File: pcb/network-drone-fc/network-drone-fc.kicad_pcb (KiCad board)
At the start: 4 copper layers, 36 x 39 mm, 84 parts, among them J1 U.FL-R-SMT-1, J2 TYPE-C 16PIN 2MD, J3 U.FL GPS, J4 ESC, J5 Sensor port 5V I2C, J6 Radio UART 5V, J7 Charging board, U1 ESP32-S3FN8, U2 USBLC6-2SC6, U3 AP63205WU-7, U4 TLV75733PDRVR, U5 TPS7A2033PDBVR, U6 ICM-42688-P, U7 BMP581, U8 MAX-M10S, X1 Q22FA12800101

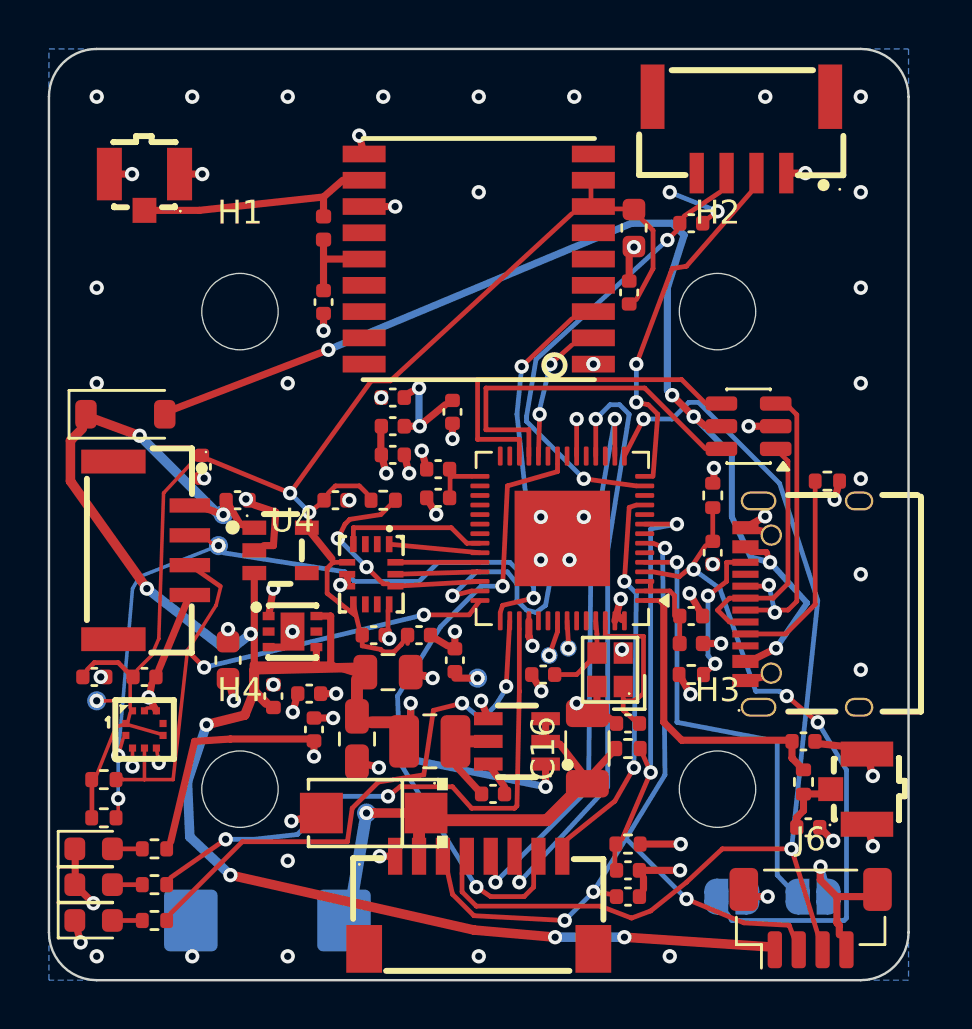
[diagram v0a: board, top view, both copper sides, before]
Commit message: PCB: chamfer the 16 right-angle track corners into 45 degree bends
USB pair, crystal, IMU interrupt, CC2 and a few power links. No corner on the board is now 100 degrees or sharper. DRC 0 errors; schematic and board still match on all 296 pins.
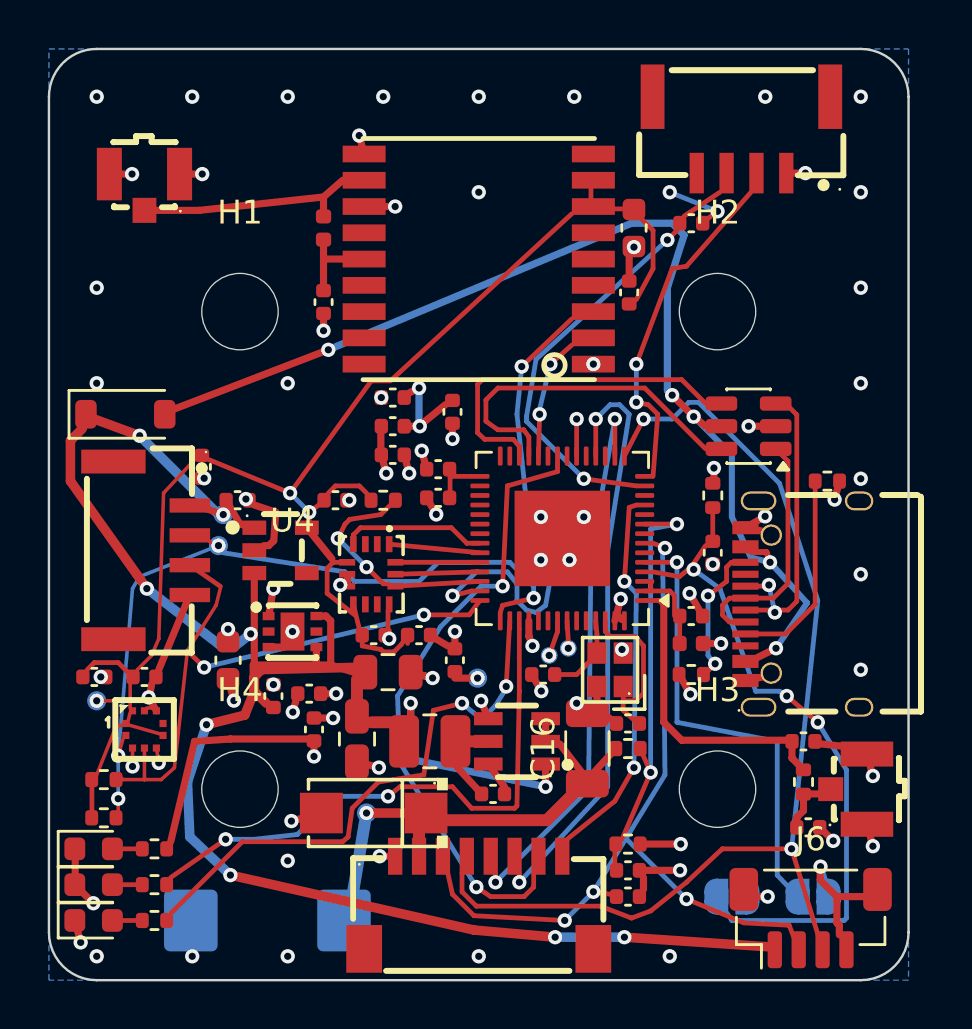
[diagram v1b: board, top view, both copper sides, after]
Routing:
- net USB_DN: track 14.9 -> 14.2 mm
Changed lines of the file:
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@@
 	)
 	(segment
-		(start 91.4 99.8)
+		(start 91.2 99.8)
 		(end 91 99.8)
 		(width 0.3)
@@
 	(segment
 		(start 91.5 98.4)
-		(end 91.4 99.8)
+		(end 91.414249 99.600508)
 		(width 0.3)
 		(layer "F.Cu")
@@
 	)
 	(segment
+		(start 91.2 99.8)
+		(end 91.414249 99.600508)
+		(width 0.3)
+		(layer "F.Cu")
+		(net 2)
+	)
+	(segment
 		(start 114.28 111.6)
 		(end 114.845685 112.165685)
@@
 	)
 	(segment
+		(start 110.212132 102.287867)
+		(end 110.212132 102.712132)
+		(width 0.2)
+		(layer "F.Cu")
+		(net 7)
+	)
+	(segment
 		(start 110.5 102)
-		(end 110 102.5)
+		(end 110.212132 102.287867)
 		(width 0.2)
 		(layer "F.Cu")
@@
 	)
 	(segment
-		(start 110 102.5)
+		(start 110.212132 102.712132)
 		(end 110.5 103)
 		(width 0.2)
@@
 	)
 	(segment
-		(start 100.3 93.2)
-		(end 100.3 94.95)
+		(start 100.3 93.7)
+		(end 100.3 94.592857)
 		(width 0.2)
 		(layer "F.Cu")
@@
 	)
 	(segment
-		(start 102.1 94.95)
+		(start 102.1 95.25)
 		(end 102.1 96.05)
 		(width 0.2)
@@
 	(segment
 		(start 106.95 93.2)
-		(end 100.3 93.2)
+		(end 100.8 93.2)
+		(width 0.2)
+		(layer "F.Cu")
+		(net 8)
+	)
+	(segment
+		(start 100.8 94.95)
+		(end 101.883333 94.95)
+		(width 0.2)
+		(layer "F.Cu")
+		(net 8)
+	)
+	(segment
+		(start 100.3 93.7)
+		(end 100.8 93.2)
 		(width 0.2)
 		(layer "F.Cu")
@@
 	)
 	(segment
-		(start 100.3 94.95)
-		(end 102.1 94.95)
+		(start 100.3 94.592857)
+		(end 100.8 94.95)
+		(width 0.2)
+		(layer "F.Cu")
+		(net 8)
+	)
+	(segment
+		(start 102.1 95.25)
+		(end 101.883333 94.95)
 		(width 0.2)
 		(layer "F.Cu")
@@
 	)
 	(segment
+		(start 100.15 92.85)
+		(end 99.95 93.05)
+		(width 0.2)
+		(layer "F.Cu")
+		(net 10)
+	)
+	(segment
 		(start 108.5 92.85)
-		(end 99.95 92.85)
+		(end 100.15 92.85)
 		(width 0.2)
 		(layer "F.Cu")
@@
 	)
 	(segment
-		(start 99.95 95.35)
-		(end 101.7 95.35)
+		(start 100.25 95.35)
+		(end 99.95 95.074)
 		(width 0.2)
 		(layer "F.Cu")
@@
 	)
 	(segment
-		(start 101.7 95.35)
+		(start 100.25 95.35)
+		(end 101.451428 95.35)
+		(width 0.2)
+		(layer "F.Cu")
+		(net 10)
+	)
+	(segment
+		(start 101.7 95.649999)
 		(end 101.7 96.05)
 		(width 0.2)
@@
 	)
 	(segment
+		(start 101.451428 95.35)
+		(end 101.7 95.649999)
+		(width 0.2)
+		(layer "F.Cu")
+		(net 10)
+	)
+	(segment
 		(start 109.5 93.85)
 		(end 108.5 92.85)
@@
 	)
 	(segment
-		(start 99.95 92.85)
-		(end 99.95 95.35)
+		(start 99.95 93.05)
+		(end 99.95 95.074)
 		(width 0.2)
 		(layer "F.Cu")
@@
 	)
 	(segment
+		(start 90.899915 104.992859)
+		(end 90.6 105.3)
+		(width 0.4)
+		(layer "F.Cu")
+		(net 11)
+	)
+	(segment
 		(start 90.6 105.9)
 		(end 90.2 106.9)
@@
 	(segment
 		(start 94.8 104.9)
-		(end 90.6 105)
+		(end 90.899915 104.992859)
 		(width 0.4)
 		(layer "F.Cu")
@@
 	(segment
 		(start 93.8 104.8)
-		(end 93.8 102.75)
+		(end 93.8 102.95)
 		(width 0.3)
 		(layer "F.Cu")
@@
 	)
 	(segment
-		(start 90.6 105)
+		(start 90.6 105.3)
 		(end 90.6 105.9)
 		(width 0.4)
@@
 	)
 	(segment
+		(start 93.8 102.95)
+		(end 93.6 102.75)
+		(width 0.3)
+		(layer "F.Cu")
+		(net 11)
+	)
+	(segment
 		(start 90 98.9)
 		(end 90.6 99.05)
@@
 	)
 	(segment
-		(start 93.8 102.75)
+		(start 93.6 102.75)
 		(end 93.2 102.75)
 		(width 0.3)
@@
 	(segment
 		(start 90.1 112.2)
-		(end 94.5 112.2)
+		(end 94.3 112.2)
 		(width 0.2)
 		(layer "F.Cu")
@@
 	)
 	(segment
-		(start 94.5 112.2)
+		(start 94.528284 112.00201)
 		(end 94.7 110.8)
 		(width 0.2)
@@
 	)
 	(segment
+		(start 94.3 112.2)
+		(end 94.528284 112.00201)
+		(width 0.2)
+		(layer "F.Cu")
+		(net 15)
+	)
+	(segment
 		(start 94.7 110.8)
 		(end 95.8 109.7)
@@
 	)
 	(segment
-		(start 110.38 100.5)
+		(start 110.38 100.7)
 		(end 110.38 101.3)
 		(width 0.2)
@@
 	(segment
 		(start 111.17 100.5)
-		(end 110.38 100.5)
+		(end 110.58 100.5)
+		(width 0.2)
+		(layer "F.Cu")
+		(net 16)
+	)
+	(segment
+		(start 110.38 100.7)
+		(end 110.58 100.5)
 		(width 0.2)
 		(layer "F.Cu")
@@
 	(segment
 		(start 98.85 99.05)
-		(end 94.75 99.05)
+		(end 95.05 99.05)
 		(width 0.2)
 		(layer "F.Cu")
@@
 	)
 	(segment
-		(start 94.75 99.05)
+		(start 95.05 99.05)
+		(end 94.75 99.35)
+		(width 0.2)
+		(layer "F.Cu")
+		(net 30)
+	)
+	(segment
+		(start 94.75 99.35)
 		(end 94.75 99.74)
 		(width 0.2)
@@
 	)
 	(segment
-		(start 87.2 109.6)
+		(start 86.7 109.6)
 		(end 86 109.6)
 		(width 0.15)
@@
 	)
 	(segment
+		(start 86.7 109.6)
+		(end 87.255215 109.103058)
+		(width 0.15)
+		(layer "F.Cu")
+		(net 35)
+	)
+	(segment
 		(start 88.5 104.9)
 		(end 87.8 104.2)
@@
 	(segment
 		(start 87.8 104.2)
-		(end 87.2 109.6)
+		(end 87.255215 109.103058)
 		(width 0.15)
 		(layer "F.Cu")
@@
 	(segment
 		(start 105.3 102.95)
-		(end 105.3 103.6)
+		(end 105.3 103.399999)
 		(width 0.2)
 		(layer "F.Cu")
@@
 	)
 	(segment
-		(start 106.9 103.6)
+		(start 106.9 104)
 		(end 106.9 106)
 		(width 0.2)
@@
 	)
 	(segment
-		(start 105.3 103.6)
-		(end 106.9 103.6)
+		(start 105.5 103.6)
+		(end 106.55 103.6)
 		(width 0.2)
 		(layer "F.Cu")
@@
 	)
 	(segment
+		(start 106.9 104)
+		(end 106.55 103.6)
+		(width 0.2)
+		(layer "F.Cu")
+		(net 42)
+	)
+	(segment
 		(start 106.05 106.3)
 		(end 106.05 105.7)
 		(width 0.2)
 		(layer "F.Cu")
+		(net 42)
+	)
+	(segment
+		(start 105.3 103.399999)
+		(end 105.5 103.6)
+		(width 0.2)
+		(layer "F.Cu")

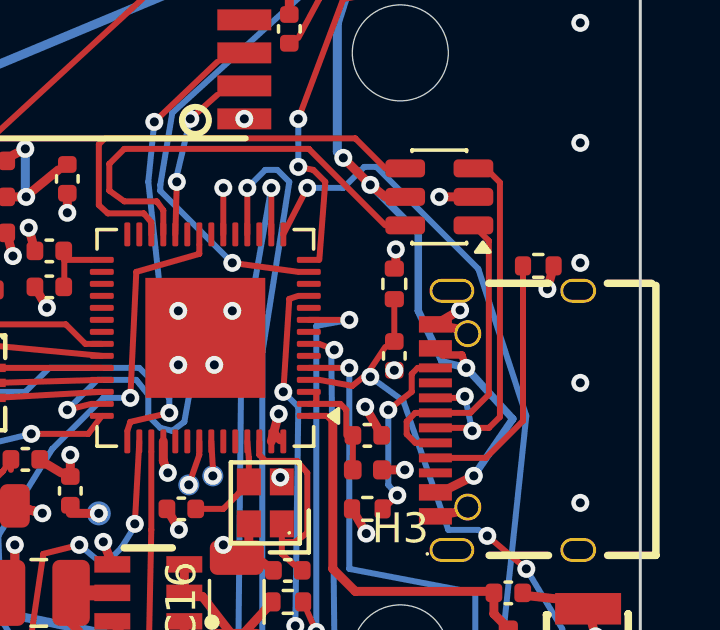
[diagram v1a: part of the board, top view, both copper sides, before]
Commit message: PCB: ground via moved clear of the USB socket's slot; footprint library links and unused-pin net names synced with the schematic
The via was 0.20 mm from the slot wall and is now 0.26 mm (fab minimum 0.25). The rest is bookkeeping with no copper change: KiCad's schematic parity check drops from 140 items to 2, both the USB socket's grounded locating pegs.
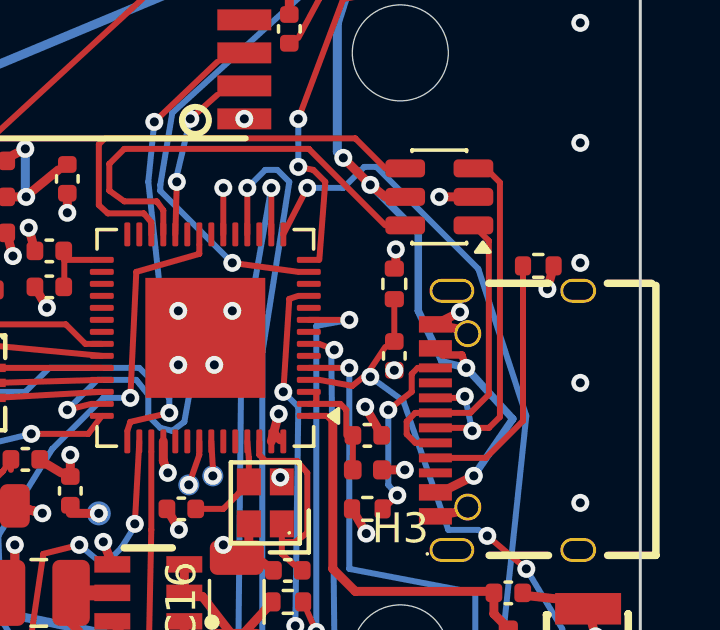
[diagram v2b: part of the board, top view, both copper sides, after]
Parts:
- C1, C10, C11, C12, C13, C14, C15, C17, C2, C20, C21, C22, C23, C24, C25, C26, C27, C28, C29, C3, C31, C32, C33, C34, C5, C6, C7, C8, C9: footprint C_0402_1005Metric -> Capacitor_SMD:C_0402_1005Metric
- C16: footprint C_1206_3216Metric -> Capacitor_SMD:C_0805_2012Metric
- C18, C19: footprint C_0805_2012Metric -> Capacitor_SMD:C_0805_2012Metric
- C30, C4: footprint C_0603_1608Metric -> Capacitor_SMD:C_0603_1608Metric
- C35: footprint CP_EIA-7343-31_Kemet-D_HandSolder -> Capacitor_Tantalum_SMD:CP_EIA-7343-31_Kemet-D_HandSolder
- D1: footprint D_SOD-123 -> Diode_SMD:D_SOD-123
- D2, D3, D4: footprint LED_0603_1608Metric -> LED_SMD:LED_0603_1608Metric
- D5: footprint SMA_L4.4-W2.6-LS5.0-RD -> tar_fc:SMA_L4.4-W2.6-LS5.0-RD
- J1, J3: footprint RF-SMD_FRF05002-JSS103M -> tar_fc:RF-SMD_FRF05002-JSS103M
- J2: footprint USB-C-SMD_TYPE-C-16PIN-2MD-073 -> tar_fc:USB-C-SMD_TYPE-C-16PIN-2MD-073
- J4: footprint CONN-TH_SM08B-SRSS-TB-LF-SN -> tar_fc:CONN-TH_SM08B-SRSS-TB-LF-SN
- J5, J7: footprint CONN-SMD_4P-P1.25_SM04B-GHS-TB-LF-SN -> tar_fc:CONN-SMD_4P-P1.25_SM04B-GHS-TB-LF-SN
- L1, L3: footprint L_0402_1005Metric -> Inductor_SMD:L_0402_1005Metric
- L2: footprint L_1008_2520Metric -> Inductor_SMD:L_1008_2520Metric
- R1, R10, R11, R12, R13, R3, R4, R5, R6, R7, R8, R9: footprint R_0402_1005Metric -> Resistor_SMD:R_0402_1005Metric
- TP1, TP2, TP3, TP4, TP5, TP6: footprint TestPoint_Pad_D1.0mm -> TestPoint:TestPoint_Pad_D1.0mm
- U1: footprint QFN-56-1EP_7x7mm_P0.4mm_EP4x4mm -> Package_DFN_QFN:QFN-56-1EP_7x7mm_P0.4mm_EP4x4mm
- U2: footprint SOT-23-6 -> Package_TO_SOT_SMD:SOT-23-6
- U3: footprint TSOT-23-6_L2.9-W1.6-P0.95-LS2.8-BL -> tar_fc:TSOT-23-6_L2.9-W1.6-P0.95-LS2.8-BL
- U4: footprint TDFN-6_L2.0-W2.0-P0.65-TL-EP -> tar_fc:TDFN-6_L2.0-W2.0-P0.65-TL-EP
- U5: footprint SOT-23-5_L2.9-W1.6-P0.95-LS2.8-BR -> tar_fc:SOT-23-5_L2.9-W1.6-P0.95-LS2.8-BR
- U6: footprint LGA-14_L3.0-W2.5-P0.50-TL -> tar_fc:LGA-14_L3.0-W2.5-P0.50-TL
- U7: footprint LGA-10_L2.0-W2.0-P0.50-TL_BMP581 -> tar_fc:LGA-10_L2.0-W2.0-P0.50-TL_BMP581
- U8: footprint SMD-18_L10.1-W9.7-P1.10-TL_SKG09F -> tar_fc:SMD-18_L10.1-W9.7-P1.10-TL_SKG09F
- X1: footprint CRYSTAL-SMD_4P-L2.0-W1.6-BL -> tar_fc:CRYSTAL-SMD_4P-L2.0-W1.6-BL
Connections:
- J2 pad A8: (no net) -> unconnected-(J2-SBU1-PadA8)
- J2 pad B8: (no net) -> unconnected-(J2-SBU2-PadB8)
- J4 pad 10: (no net) -> unconnected-(J4-Pad10)
- J4 pad 9: (no net) -> unconnected-(J4-Pad9)
- J5 pad 5: (no net) -> unconnected-(J5-Pad5)
- J5 pad 6: (no net) -> unconnected-(J5-Pad6)
- J7 pad 4: (no net) -> unconnected-(J7-Pad4)
- J7 pad 5: (no net) -> unconnected-(J7-Pad5)
- J7 pad 6: (no net) -> unconnected-(J7-Pad6)
- U1 pad 10: (no net) -> unconnected-(U1-GPIO5-Pad10)
- U1 pad 12: (no net) -> unconnected-(U1-GPIO7-Pad12)
- U1 pad 17: (no net) -> unconnected-(U1-GPIO12-Pad17)
- U1 pad 19: (no net) -> unconnected-(U1-GPIO14-Pad19)
- U1 pad 21: (no net) -> unconnected-(U1-XTAL_32K_P-Pad21)
- U1 pad 23: (no net) -> unconnected-(U1-GPIO17-Pad23)
- U1 pad 27: (no net) -> unconnected-(U1-GPIO21-Pad27)
- U1 pad 28: (no net) -> unconnected-(U1-SPICS1-Pad28)
- U1 pad 30: (no net) -> unconnected-(U1-SPIHD-Pad30)
- U1 pad 31: (no net) -> unconnected-(U1-SPIWP-Pad31)
- U1 pad 32: (no net) -> unconnected-(U1-SPICS0-Pad32)
- U1 pad 33: (no net) -> unconnected-(U1-SPICLK-Pad33)
- U1 pad 34: (no net) -> unconnected-(U1-SPIQ-Pad34)
- U1 pad 35: (no net) -> unconnected-(U1-SPID-Pad35)
- U1 pad 47: (no net) -> unconnected-(U1-MTDI-Pad47)
- U1 pad 48: (no net) -> unconnected-(U1-MTMS-Pad48)
- U1 pad 51: (no net) -> unconnected-(U1-GPIO45-Pad51)
- U1 pad 52: (no net) -> unconnected-(U1-GPIO46-Pad52)
- U1 pad 6: (no net) -> unconnected-(U1-GPIO1-Pad6)
- U1 pad 8: (no net) -> unconnected-(U1-GPIO3-Pad8)
- U4 pad 2: (no net) -> unconnected-(U4-NC-Pad2)
- U4 pad 5: (no net) -> unconnected-(U4-NC-Pad5)
- U5 pad 4: (no net) -> unconnected-(U5-NC-Pad4)
- U6 pad 10: (no net) -> unconnected-(U6-RESV-Pad10)
- U6 pad 2: (no net) -> unconnected-(U6-RESV-Pad2)
- U6 pad 3: (no net) -> unconnected-(U6-RESV-Pad3)
- U6 pad 9: (no net) -> unconnected-(U6-INT2/FSYNC/CLKIN-Pad9)
- U7 pad 7: (no net) -> unconnected-(U7-INT-Pad7)
- U8 pad 13: (no net) -> unconnected-(U8-LNA_EN-Pad13)
- U8 pad 15: (no net) -> unconnected-(U8-VIO_SEL-Pad15)
- U8 pad 16: (no net) -> unconnected-(U8-SDA-Pad16)
- U8 pad 17: (no net) -> unconnected-(U8-SCL-Pad17)
- U8 pad 18: (no net) -> unconnected-(U8-SAFEBOOT_N-Pad18)
- U8 pad 4: (no net) -> unconnected-(U8-TIMEPULSE-Pad4)
- U8 pad 5: (no net) -> unconnected-(U8-EXTINT-Pad5)
- U8 pad 6: (no net) -> unconnected-(U8-V_BCKP-Pad6)
- U8 pad 9: (no net) -> unconnected-(U8-RESET_N-Pad9)

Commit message: Schematic: C16 footprint field set to 1206 to match the board
The board has carried the 1206 since the capacitor was enlarged; the schematic's footprint field still named the 0805. No copper change.
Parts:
- C16: footprint Capacitor_SMD:C_0805_2012Metric -> Capacitor_SMD:C_1206_3216Metric
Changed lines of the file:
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@@
 		)
 	)
-	(footprint "Capacitor_SMD:C_0805_2012Metric"
+	(footprint "Capacitor_SMD:C_1206_3216Metric"
 		(layer "F.Cu")
 		(at 104.55 108.3 90)

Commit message: PCB: 7-pin JST-SH charging connector and top-entry landing sensor port placed and routed; GPIO7 drives charge disable
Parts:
- added J8: Landing sensor 5V I2C, tar_fc:JST_SH_BM04B-SRSS-TB_1x04_Vertical, F.Cu at (115.3, 89.5)
- J7: footprint tar_fc:CONN-SMD_4P-P1.25_SM04B-GHS-TB-LF-SN -> tar_fc:JST_SH_SM07B-SRSS-TB_1x07_Horizontal
- R12, R13: value 4.7k -> 2.2k
- moved J7 0.67 mm to (111.5, 82.2)
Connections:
- C34 pad 1: AUX_ADC -> CHG_STAT
- J7 pad 1: GND -> VBAT
- J7 pad 2: DOCK_DET -> GND
- J7 pad 3: AUX_ADC -> I2C_SDA
- J7 pad 4: unconnected-(J7-Pad4) -> I2C_SCL
- J7 pad 5: unconnected-(J7-Pad5) -> CHG_PG
- J7 pad 6: unconnected-(J7-Pad6) -> CHG_STAT
- U1 pad 12: unconnected-(U1-GPIO7-Pad12) -> CHG_CD
- U1 pad 13: AUX_ADC -> CHG_STAT
- U1 pad 14: DOCK_DET -> CHG_PG
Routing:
- net I2C_SDA: track 26.5 -> 100.9 mm, vias 2 -> 4
- net I2C_SCL: track 30.8 -> 93.5 mm, vias 4 -> 5
- net VBAT: track 20.1 -> 75.0 mm, vias 1 -> 2
- net +5V: track 86.4 -> 115.6 mm, vias 10 -> 12
- net AUX_ADC: track 18.0 -> 0.00 mm, vias 2 -> 0
- net CHG_STAT: track 0.00 -> 17.6 mm, vias 0 -> 2
- net CHG_CD: track 0.00 -> 17.5 mm, vias 0 -> 2
- net DOCK_DET: track 14.3 -> 0.00 mm, vias 2 -> 0
- net CHG_PG: track 0.00 -> 14.2 mm, vias 0 -> 2
- net GND: track 61.0 -> 63.9 mm, vias 81 -> 77
- net ESC_TELEM: track 45.1 -> 45.5 mm, vias 2 -> 4
